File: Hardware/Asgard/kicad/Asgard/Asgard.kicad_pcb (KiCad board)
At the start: 2 copper layers, 4 parts, among them J1 CONN_01X04, J2 CONN_01X04, J3 CONN_01X06, U1 Teensy3.6fsocket

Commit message: Proposal Asgard Schematics
Ready for routing
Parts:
- removed J1, J2: CONN_01X04, Socket_Strips:Socket_Strip_Angled_1x04_Pitch2.54mm
- removed J3: CONN_01X06, Socket_Strips:Socket_Strip_Straight_1x06_Pitch2.54mm
- removed U1: Teensy3.6fsocket, Teensy:Socket_Strip_Teensy3.6_2x24_Pitch2.54mm
- added ABSP1: CONN_01X04, Socket_Strips:Socket_Strip_Angled_1x04_Pitch2.54mm, B.Cu at (151.1, 73.7)
- added BLUESMIRF1: CONN_01X06, Socket_Strips:Socket_Strip_Straight_1x06_Pitch2.54mm, B.Cu at (141.0, 124.5)
- added DELTAP1: CONN_01X04, Socket_Strips:Socket_Strip_Angled_1x04_Pitch2.54mm, B.Cu at (151.1, 100.3)
- added OAT1: CONN_01X03, Pin_Headers:Pin_Header_Angled_1x03_Pitch2.54mm, F.Cu at (144.8, 69.8)
- added R1: 4700, Resistors_SMD:R_1206, F.Cu at (147.3, 77.5)
- added R2: 4700, Resistors_SMD:R_1206, F.Cu at (147.3, 86.4)
- added R3: 4700, Resistors_SMD:R_1206, F.Cu at (147.3, 94.0)
- added R4: 4700, Resistors_SMD:R_1206, F.Cu at (147.3, 110.5)
- added TEENSYV3.6: Teensy3.6fsocket, Teensy:Socket_Strip_Teensy3.6_2x24_Pitch2.54mm, F.Cu at (147.2, 61.8)
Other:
- board outline added: 20.3 x 67.3 mm

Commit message: PCB Preliminary Layout
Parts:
- OAT1: moved to B.Cu
- moved R1 33.0 mm to (147.3, 110.5)
- moved R4 31.8 mm to (147.3, 78.7)
- moved DELTAP1 20.5 mm to (143.5, 119.4), turned to 270 degrees
- moved R2 12.7 mm to (147.3, 99.1)
- moved OAT1 5.11 mm to (149.9, 70.4)
- moved R3 5.08 mm to (147.3, 88.9)
- moved BLUESMIRF1 0.51 mm to (141.0, 125.0)
- moved TEENSYV3.6 0.37 mm to (147.3, 61.5)
- moved ABSP1 0.36 mm to (150.9, 73.9)
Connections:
- net Net-(ABSP1-Pad1) renamed GND
- net Net-(ABSP1-Pad2) renamed +3V3
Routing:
- net +3V3: track 0.00 -> 70.9 mm
- net Net-(BLUESMIRF1-Pad3): track 0.00 -> 68.7 mm, vias 0 -> 1
- net Net-(BLUESMIRF1-Pad2): track 0.00 -> 60.3 mm
- net Net-(DELTAP1-Pad3): track 0.00 -> 49.1 mm, vias 0 -> 3
- net Net-(ABSP1-Pad4): track 0.00 -> 48.5 mm, vias 0 -> 5
- net Net-(DELTAP1-Pad4): track 0.00 -> 46.6 mm, vias 0 -> 3
- net Net-(ABSP1-Pad3): track 0.00 -> 38.3 mm, vias 0 -> 1
- net Net-(OAT1-Pad2): track 0.00 -> 28.7 mm, vias 0 -> 1
- added copper zone on F.Cu, net GND
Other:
- net class Default: clearance 0.2 -> 0.3; trace_width 0.25 -> 0.5
- net class power added: clearance 0.4, trace_width 0.6, via_dia 0.8, via_drill 0.6
- rule trace_clearance: 0.2 -> 0.3
- rule trace_min: 0.2 -> 0.4

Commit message: PCB-Init Commit
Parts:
- moved ABSP1 0.51 mm to (151.4, 73.9)
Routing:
- net GND: track 0.00 -> 78.9 mm
- net Net-(ABSP1-Pad4): track 48.5 -> 42.6 mm, vias 5 -> 2
- net Net-(OAT1-Pad2): track 28.7 -> 29.9 mm
- net Net-(BLUESMIRF1-Pad2): track 60.3 -> 60.5 mm, vias 0 -> 1
- net Net-(DELTAP1-Pad3): track 49.1 -> 48.9 mm, vias 3 -> 5
- net Net-(DELTAP1-Pad4): vias 3 -> 5
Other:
- net class power removed

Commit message: Updated Schematics
Addedd indication for HC-05/HC-06 Compatibility
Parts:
- removed ABSP1, DELTAP1: CONN_01X04, Socket_Strips:Socket_Strip_Angled_1x04_Pitch2.54mm
- removed BLUESMIRF1: CONN_01X06, Socket_Strips:Socket_Strip_Straight_1x06_Pitch2.54mm
- removed OAT1: CONN_01X03, Pin_Headers:Pin_Header_Angled_1x03_Pitch2.54mm
- removed R1, R2, R3, R4: 4700, Resistors_SMD:R_1206
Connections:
- TEENSYV3.6 pad 25: +3V3 -> Net-(TEENSYV3.6-Pad25)
- TEENSYV3.6 pad 27: Net-(TEENSYV3.6-Pad27) -> +3V3
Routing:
- net GND: track 78.9 -> 0.00 mm
- net +3V3: track 70.5 -> 0.00 mm
- net Net-(BLUETOOTH1-Pad2): track 68.7 -> 0.00 mm, vias 1 -> 0
- net Net-(BLUETOOTH1-Pad1): track 60.5 -> 0.00 mm, vias 1 -> 0
- net Net-(DELTAP1-Pad3): track 48.9 -> 0.00 mm, vias 5 -> 0
- net Net-(DELTAP1-Pad4): track 46.6 -> 0.00 mm, vias 5 -> 0
- net Net-(ABSP1-Pad4): track 42.6 -> 0.00 mm, vias 2 -> 0
- net Net-(ABSP1-Pad3): track 38.3 -> 0.00 mm, vias 1 -> 0
- net Net-(OAT1-Pad2): track 29.9 -> 0.00 mm, vias 1 -> 0

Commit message: Fiddling with packages
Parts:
- added ABSP1: CONN_01X04, Socket_Strips:Socket_Strip_Straight_1x04_Pitch2.54mm, F.Cu at (144.8, 78.7)
- added BLUETOOTH1: CONN_01X04, Socket_Strips:Socket_Strip_Straight_1x04_Pitch2.54mm, F.Cu at (144.8, 104.1)
- added DELTAP1: CONN_01X04, Socket_Strips:Socket_Strip_Straight_1x04_Pitch2.54mm, F.Cu at (149.9, 87.6)
- added OAT1: CONN_01X03, Pin_Headers:Pin_Header_Angled_1x03_Pitch2.54mm, F.Cu at (171.4, 114.3)
- added R1: 4700, Resistors_THT:R_Axial_DIN0204_L3.6mm_D1.6mm_P5.08mm_Horizontal, F.Cu at (144.8, 66.0)
- added R2, R3, R4: 4700, Resistors_THT:R_Axial_DIN0204_L3.6mm_D1.6mm_P5.08mm_Horizontal, F.Cu at (147.3, 137.1)

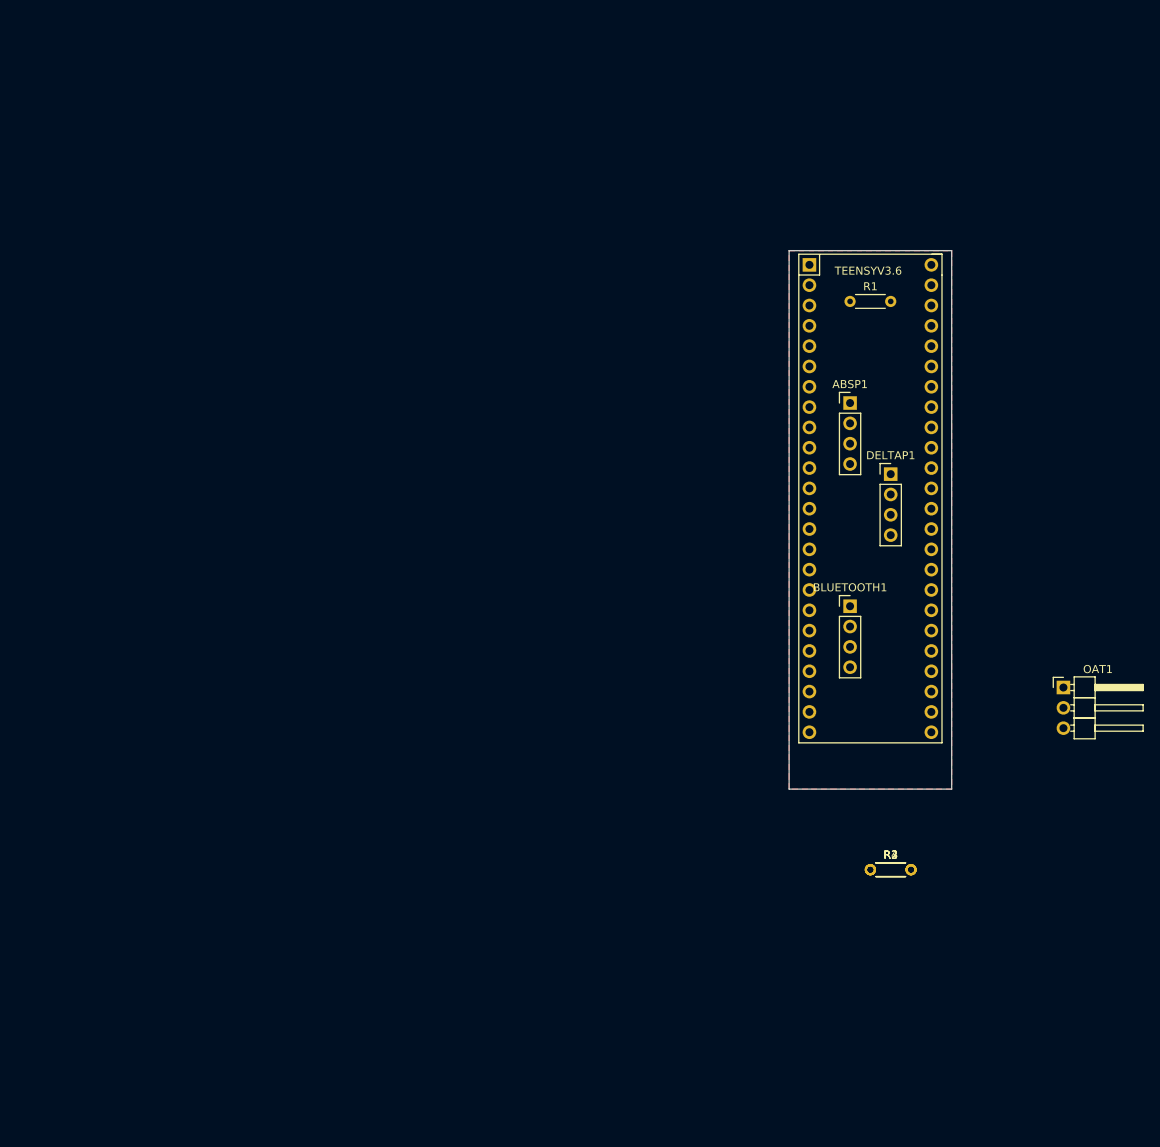
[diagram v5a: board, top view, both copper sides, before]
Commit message: Added doc
Schematics pdf
New PCB laysout started
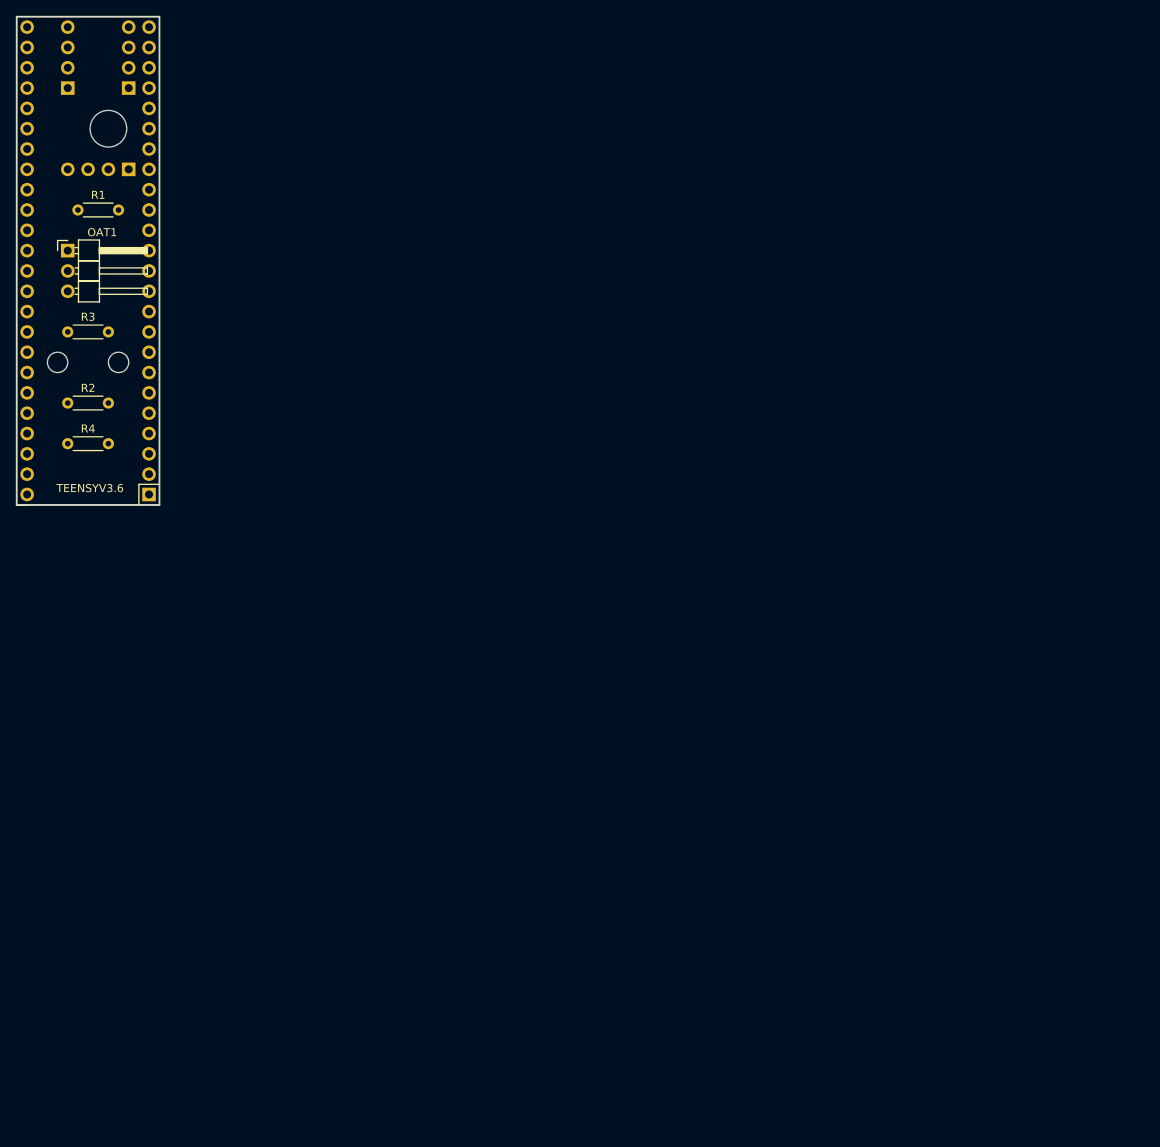
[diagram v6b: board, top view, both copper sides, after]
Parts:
- ABSP1, BLUETOOTH1, DELTAP1: moved to B.Cu
- moved OAT1 135.9 mm to (47.0, 59.7)
- moved R3 120.8 mm to (47.0, 69.8)
- moved R2 116.1 mm to (47.0, 78.7)
- moved DELTAP1 113.6 mm to (47.0, 39.4)
- moved R4 113.6 mm to (47.0, 83.8)
- moved BLUETOOTH1 105.4 mm to (54.6, 49.5), turned to 90 degrees
- moved TEENSYV3.6 101.9 mm to (49.5, 90.2), turned to 180 degrees
- moved ABSP1 98.4 mm to (54.6, 39.4)
- moved R1 97.2 mm to (48.3, 54.6)
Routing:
- removed copper zone on F.Cu, net GND
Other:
- board size 20.3 x 67.3 mm -> 17.8 x 61 mm
- board text added: "TEENSY SIDE"

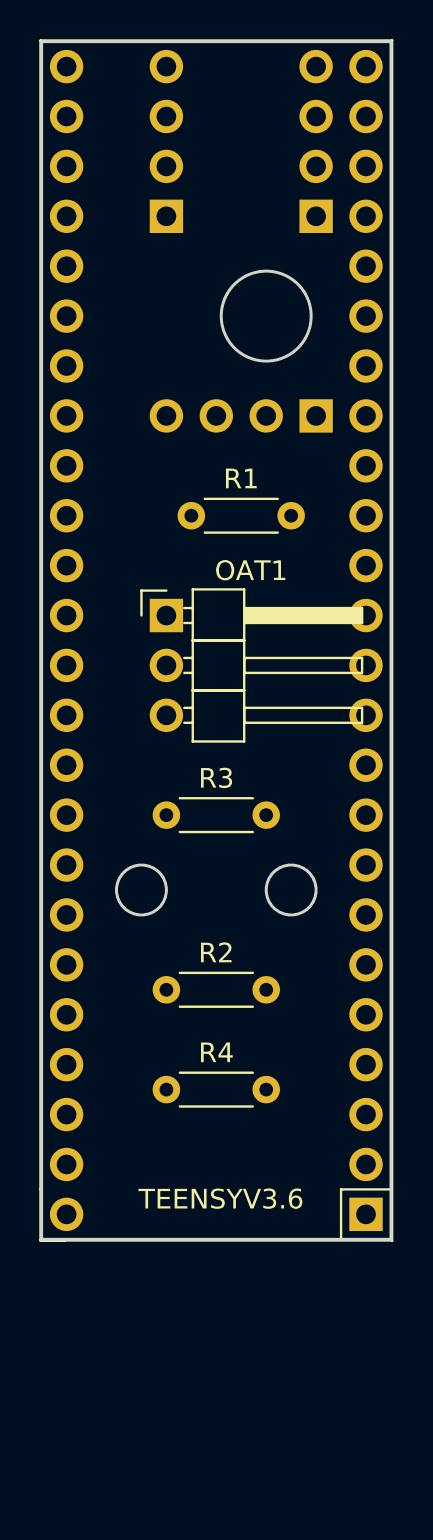
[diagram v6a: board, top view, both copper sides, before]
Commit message: Schematics update
GPIO connector is hard to place
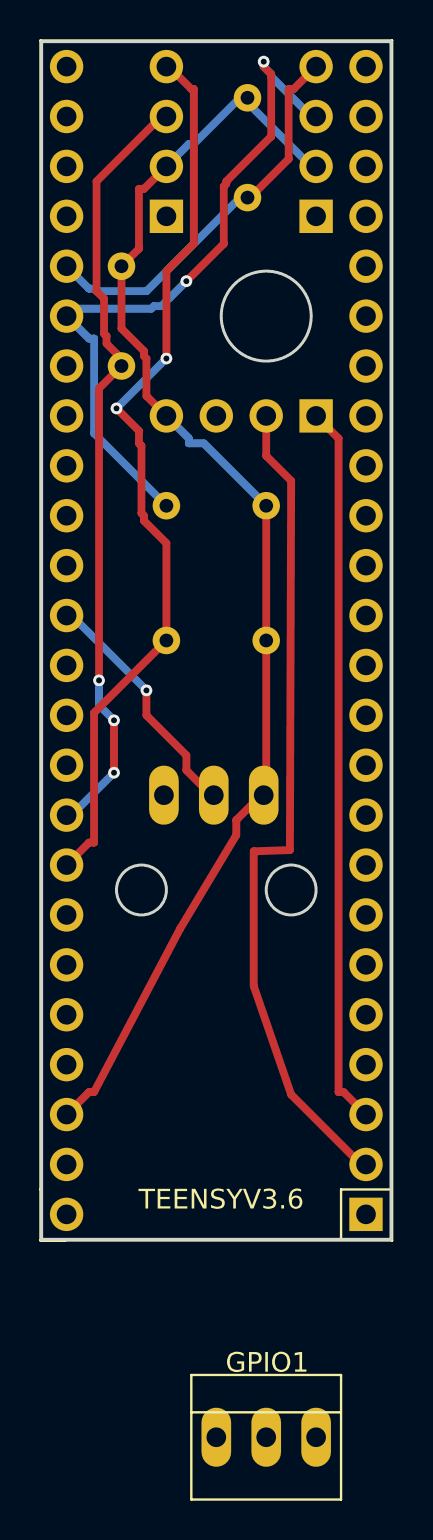
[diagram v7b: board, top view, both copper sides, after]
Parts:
- added GPIO1: CONN_01X03, Connect:PINHEAD1-3, F.Cu at (49.5, 101.5)
- OAT1: footprint Pin_Headers:Pin_Header_Angled_1x03_Pitch2.54mm -> Connect:PINHEAD1-3; moved to B.Cu
- R1, R2, R3, R4: moved to B.Cu
- moved R4 45.6 mm to (51.1, 38.4), turned to 90 degrees
- moved R2 17.8 mm to (47.0, 61.0)
- moved R3 15.7 mm to (47.0, 54.1)
- moved OAT1 10.4 mm to (51.9, 68.8), turned to 180 degrees
- moved R1 8.41 mm to (44.7, 47.0), turned to 90 degrees
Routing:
- net +3V3: track 0.00 -> 66.9 mm
- net Net-(DELTAP1-Pad4): track 0.00 -> 46.3 mm, vias 0 -> 2
- net Net-(BLUETOOTH1-Pad2): track 0.00 -> 42.5 mm
- net Net-(DELTAP1-Pad3): track 0.00 -> 39.6 mm, vias 0 -> 3
- net Net-(BLUETOOTH1-Pad1): track 0.00 -> 36.8 mm
- net Net-(ABSP1-Pad3): track 0.00 -> 35.9 mm, vias 0 -> 2
- net Net-(ABSP1-Pad4): track 0.00 -> 20.2 mm
- net Net-(OAT1-Pad2): track 0.00 -> 12.3 mm, vias 0 -> 1
- added copper zone on B.Cu, net GND
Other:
- net class Default: trace_width 0.5 -> 0.4

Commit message: PCB Rel 1
First Release of PCB
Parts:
- removed GPIO1: CONN_01X03, Connect:PINHEAD1-3
- moved OAT 1.55 mm to (52.2, 67.3)
- renumbered ABSP1 to ABSP, BLUETOOTH1 to BLUETOOTH, DELTAP1 to DELTAP, OAT1 to OAT
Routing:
- net GND: track 0.00 -> 18.8 mm
- net Net-(BLUETOOTH1-Pad2): track 42.5 -> 43.6 mm
- net Net-(OAT1-Pad2): track 12.3 -> 11.3 mm
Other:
- board text added: "GND"
- board text added: "S"
- board text added: "VCC"
